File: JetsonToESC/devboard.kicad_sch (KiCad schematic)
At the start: 6 parts, among them U1 ESP32-C3_SUPERMINI_TH

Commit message: Start On this Branch
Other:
- moved on the sheet: R4, R5, R6, R7, R8, U1

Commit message: updated too
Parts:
- added U4: MCP23018x-x-SS, Package_SO:SSOP-24_5.3x8.2mm_P0.65mm, symbol Interface_Expansion:MCP23018x-x-SS
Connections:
- net LED_TEMP is gone; now on net LED_BATT_LOW: R8.1
- net 5V: now also U4.10 (V_{DD})
- net BUTTON_100%: now also U4.22 (GPA5); no longer U1.20 (GPIO20)
- net BUTTON_25%: now also U4.19 (GPA2); no longer U1.8 (GPIO8)
- net BUTTON_50%: now also U4.20 (GPA3); no longer U1.9 (GPIO9)
- net BUTTON_75%: now also U4.21 (GPA4); no longer U1.10 (GPIO10)
- net BUTTON_STOP: now also U4.18 (GPA1); no longer U1.7 (GPIO7)
- net GND: now also U4.1 (V_{SS})
- net LED_BATT_LOW: no longer R4.1
- net LED_BATT_MED: now also R7.1; no longer R5.1
- net LED_OVERCURRENT: now also R4.1, R5.1; no longer R7.1
- net at R7.2: now also U4.8 (GPB6); no longer U1.4 (GPIO4)
- net at R6.2: now also U4.7 (GPB5); no longer U1.3 (GPIO3)
- net at R4.2: now also U4.5 (GPB3); no longer U1.1 (GPIO1)
- net at R5.2: now also U4.6 (GPB4); no longer U1.2 (GPIO2)
- net at R8.2: now also U4.9 (GPB7); no longer U1.6 (GPIO6)
- new net I2C_SCL: U1.9 (GPIO9), U4.11 (SCL)
- new net I2C_SDA: U1.8 (GPIO8), U4.12 (SDA)
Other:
- moved on the sheet: R4, R5, R6, R7, R8, U1

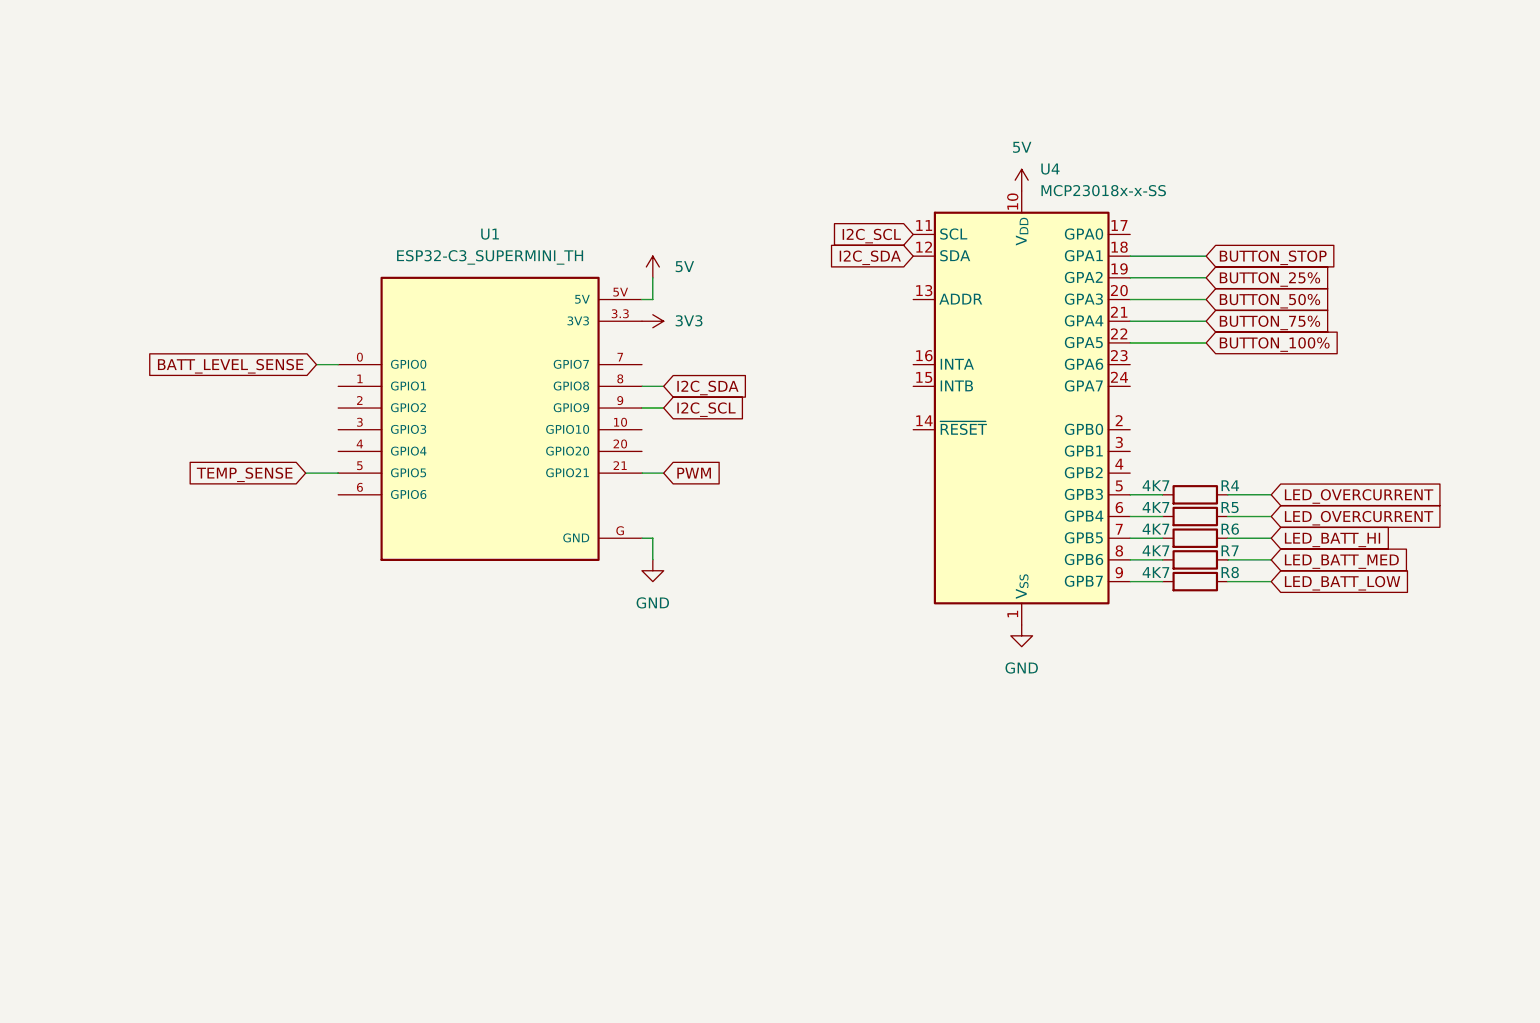
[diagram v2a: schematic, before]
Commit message: Updated routing for IO Expander and Hall Sensor
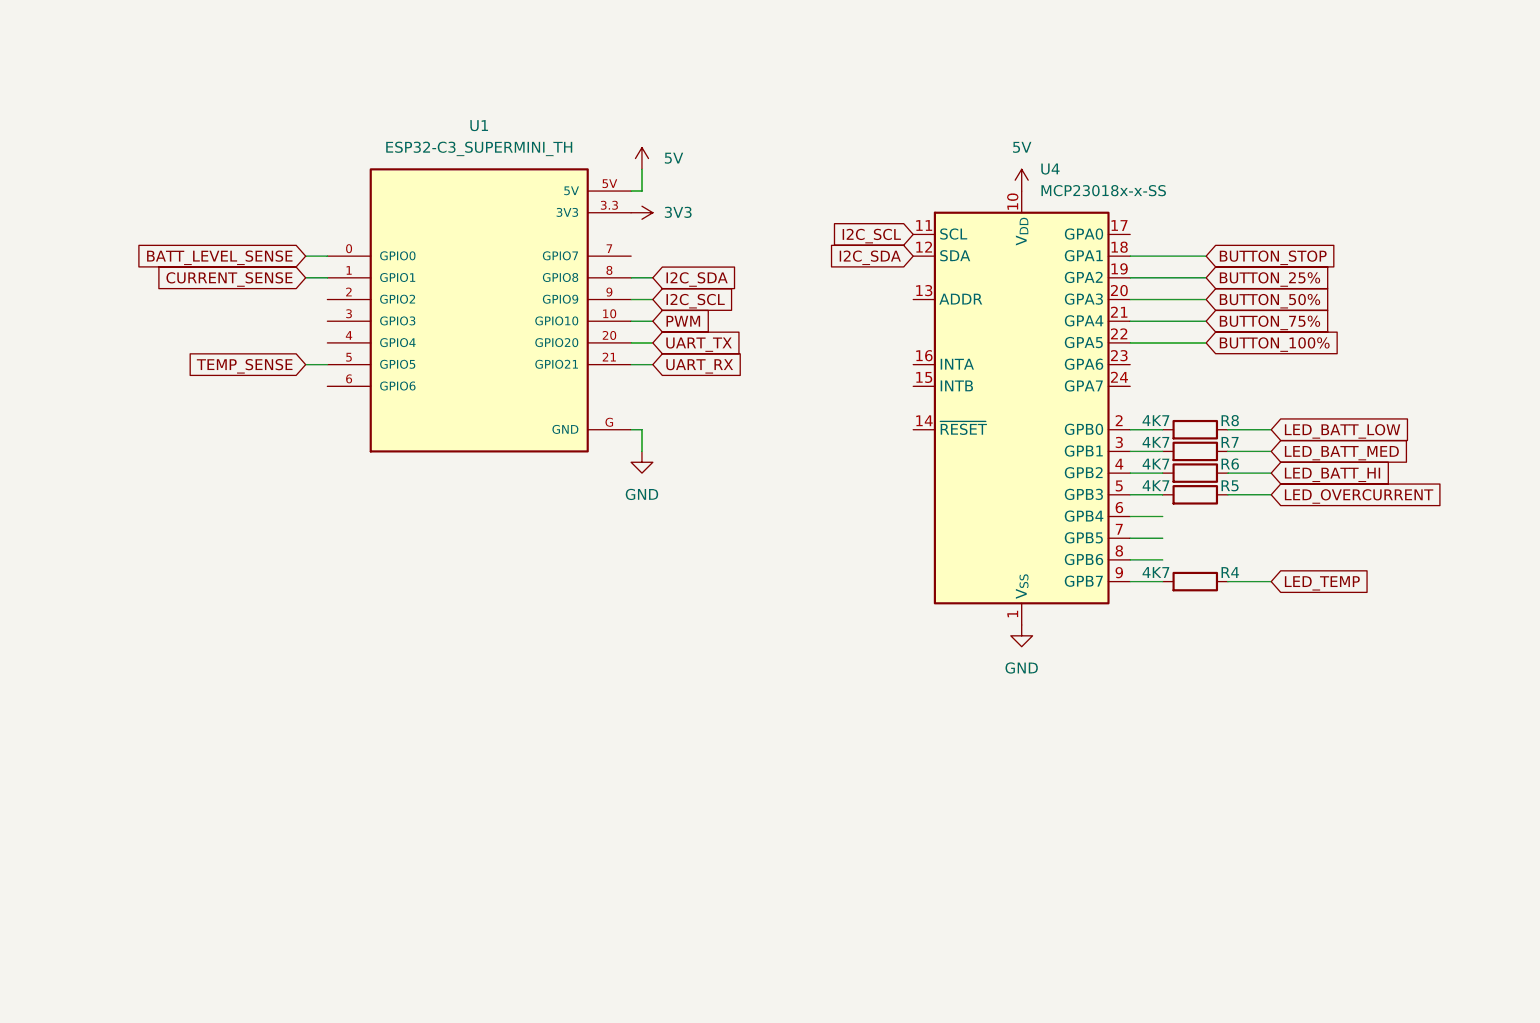
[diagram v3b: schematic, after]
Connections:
- net LED_OVERCURRENT: no longer R4.1
- net PWM: now also U1.10 (GPIO10); no longer U1.21 (GPIO21)
- net at R7.2: now also U4.3 (GPB1); no longer U4.8 (GPB6)
- net at R6.2: now also U4.4 (GPB2); no longer U4.7 (GPB5)
- net at U4.2 (GPB0): now also R8.2
- net at U4.5 (GPB3): now also R5.2; no longer R4.2
- net at U4.6 (GPB4): no longer R5.2
- net at U4.9 (GPB7): now also R4.2; no longer R8.2
- net CURRENT_SENSE: now reaches U1.1 (GPIO1)
- net UART_TX: now reaches U1.20 (GPIO20)
- new net LED_TEMP: R4.1
- new net UART_RX: U1.21 (GPIO21)
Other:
- moved on the sheet: R4, R5, R6, R7, R8, U1

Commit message: Routed I2C pullups and Reset Added ESP32c3pinout image
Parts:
- added R14, R15: 4K7, Resistor_SMD:R_0603_1608Metric, symbol Device:R
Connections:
- net 3V3: now also R14.2, R15.2
- net GND: now also U4.13 (ADDR)
- net I2C_SCL: now also R14.1
- net I2C_SDA: now also R15.1
- net I2C_RESET: now reaches U4.14 (~{RESET})
- net I2C_RESET: now also U1.7 (GPIO7)
- no-connect marks 0 -> 7

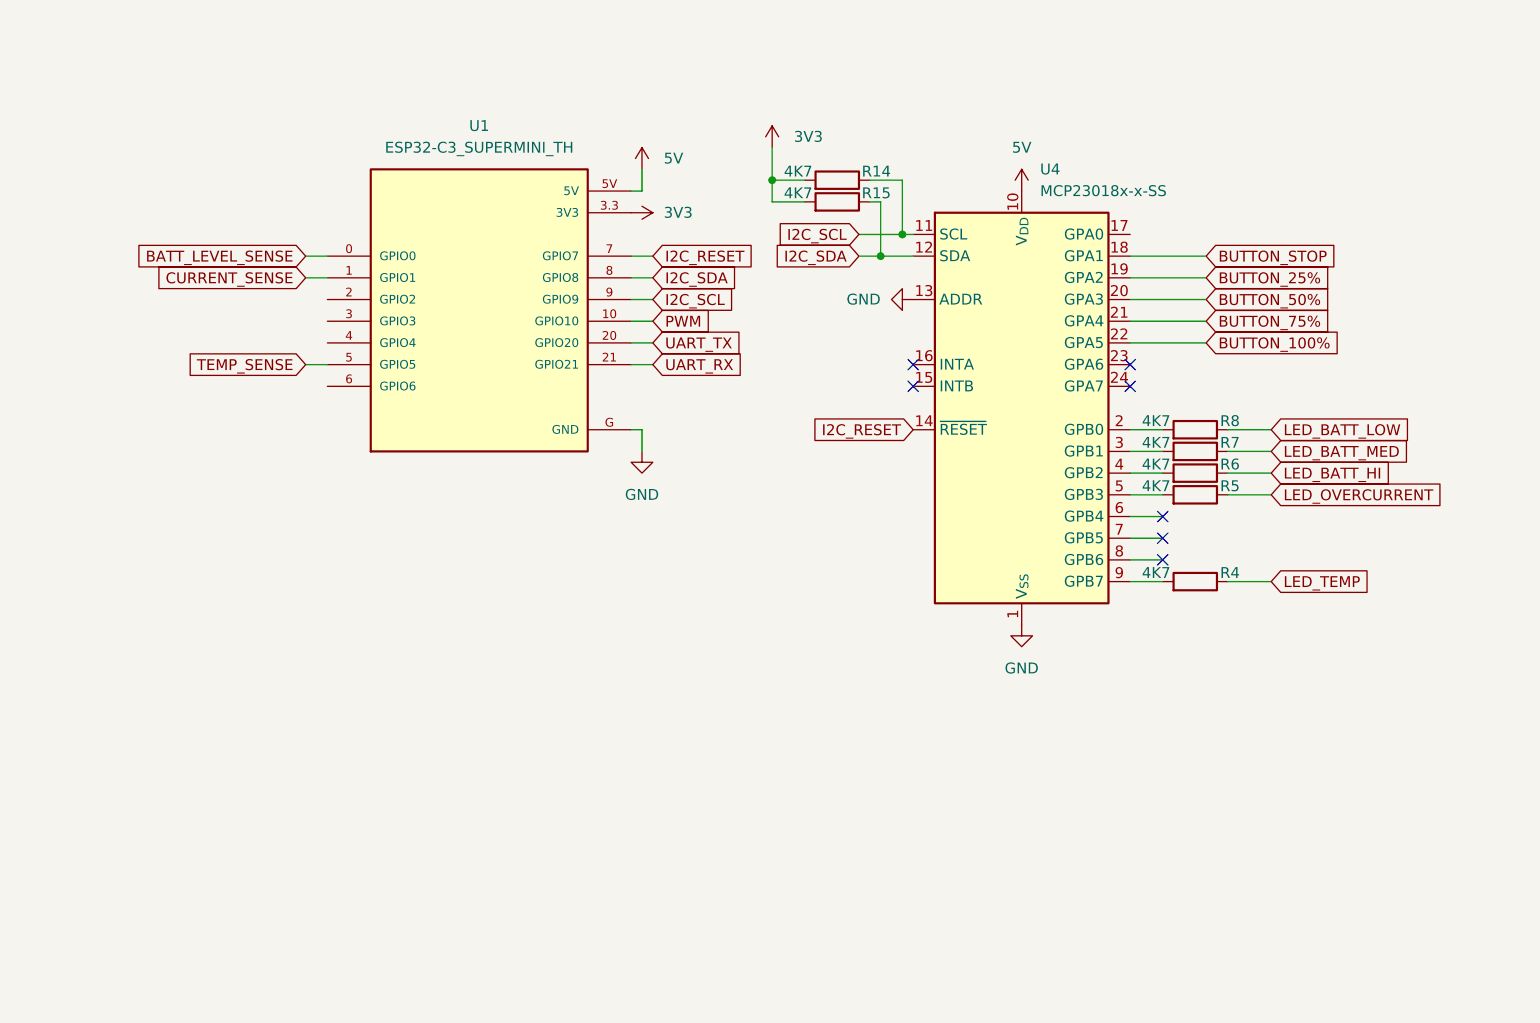
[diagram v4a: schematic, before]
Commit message: Design almost finished, added vias array for grounding too
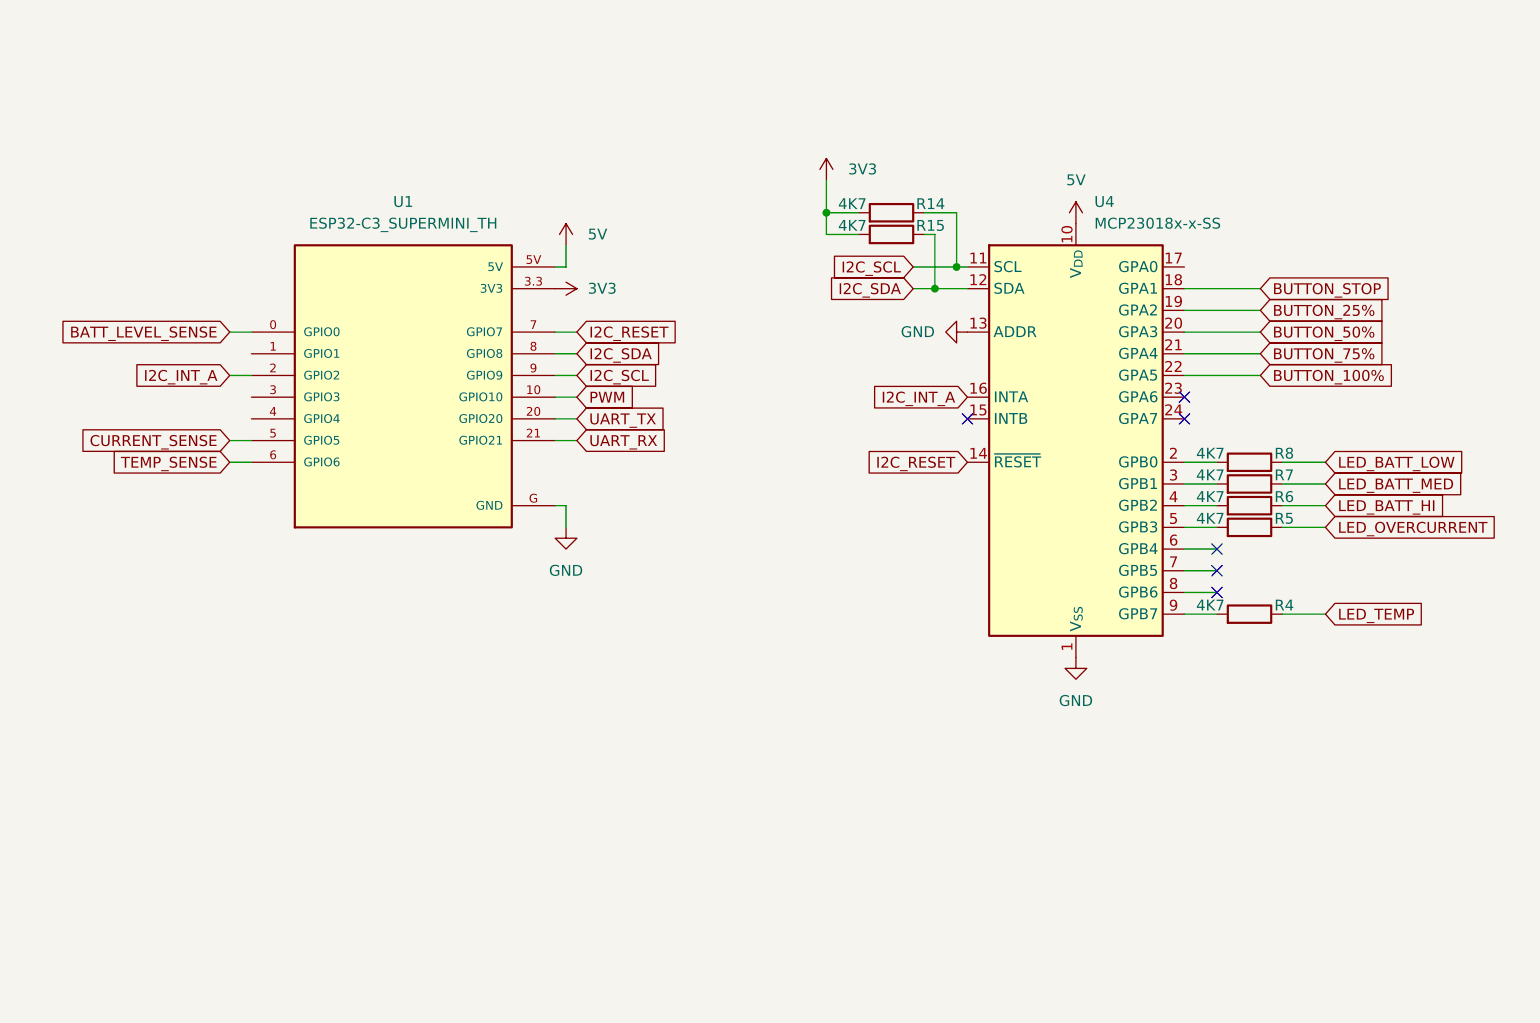
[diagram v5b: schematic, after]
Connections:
- net CURRENT_SENSE: now also U1.5 (GPIO5); no longer U1.1 (GPIO1)
- net TEMP_SENSE: now also U1.6 (GPIO6); no longer U1.5 (GPIO5)
- net I2C_INT_A: now reaches U4.16 (INTA)
- net I2C_INT_A: now also U1.2 (GPIO2)
- no-connect marks 7 -> 6
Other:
- moved on the sheet: R14, R15, R4, R5, R6, R7, R8, U1, U4

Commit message: Design and routing done
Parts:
- added C5, C6: 100nF, Capacitor_SMD:C_0603_1608Metric, symbol Device:C_Small
- added R16, R17: 4K7, Resistor_SMD:R_0603_1608Metric, symbol Device:R
- added U6: ULN2003, Package_SO:TSSOP-16_4.4x5mm_P0.65mm, symbol Transistor_Array:ULN2003
- R4: value 4K7 -> 120
- R5: renamed from R8; value 4K7 -> 120
- R6: renamed from R7; value 4K7 -> 120
- R7: renamed from R6; value 4K7 -> 120
- R8: renamed from R5; value 4K7 -> 120
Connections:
- net 3V3: now also R16.2, R17.2
- net 5V: now also C5.1, C6.1, U6.9 (COM)
- net BATT_LEVEL_SENSE: now also U1.1 (GPIO1); no longer U1.0 (GPIO0)
- net GND: now also C5.2, C6.2, U6.8 (GND)
- net I2C_INT_A: now also R16.1
- net I2C_RESET: now also U1.10 (GPIO10), R17.1; no longer U1.7 (GPIO7)
- net LED_BATT_HI: now also R6.1; no longer R7.1
- net LED_BATT_LOW: now also R8.1; no longer R5.1
- net LED_BATT_MED: now also R7.1; no longer R6.1
- net LED_OVERCURRENT: now also R5.1; no longer R8.1
- net PWM: now also U1.7 (GPIO7); no longer U1.10 (GPIO10)
- net at R6.2: now also U6.15 (O2); no longer U4.3 (GPB1)
- net at R7.2: now also U6.14 (O3); no longer U4.4 (GPB2)
- net at R5.2: now also U6.16 (O1); no longer U4.2 (GPB0)
- net at R8.2: now also U6.13 (O4); no longer U4.5 (GPB3)
- net OVERCURRENT: now reaches U4.6 (GPB4)
- net OVERCURRENT: now also U6.1 (I1)
- net at U4.9 (GPB7): no longer R4.2
- new net: R4.2, U6.12 (O5)
- new net BATT_HI: U4.5 (GPB3), U6.2 (I2)
- new net BATT_LOW: U4.3 (GPB1), U6.4 (I4)
- new net BATT_MED: U4.4 (GPB2), U6.3 (I3)
- new net TEMP: U4.2 (GPB0), U6.5 (I5)
- no-connect marks 6 -> 10
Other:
- moved on the sheet: R14, R15, R5, R6, R7, R8, U1, U4

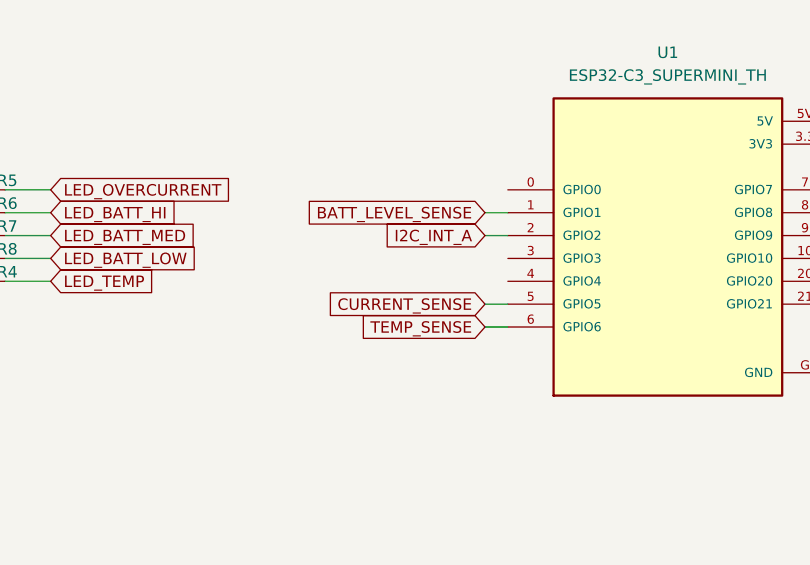
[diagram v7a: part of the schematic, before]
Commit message: Rerouted current sense signal from GPIO5 (ADC2) to GPIO3(ADC1) to avoid errata on ESP32c3
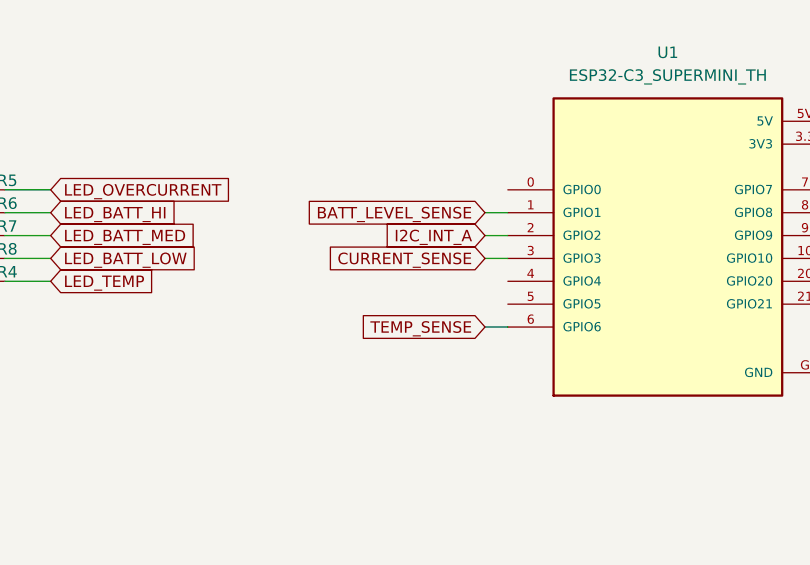
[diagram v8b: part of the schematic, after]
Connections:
- net CURRENT_SENSE: now also U1.3 (GPIO3); no longer U1.5 (GPIO5)
